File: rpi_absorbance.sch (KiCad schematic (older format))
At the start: 31 parts, among them P1 CONN_01X02, P2 CONN_01X06, P3 RPI_HEADER, Q1 NPN, U1 R-78B5.0-1.5L, U2 MEE1S1212SC, U3 DRV8825, U4 TCA9406DCUR

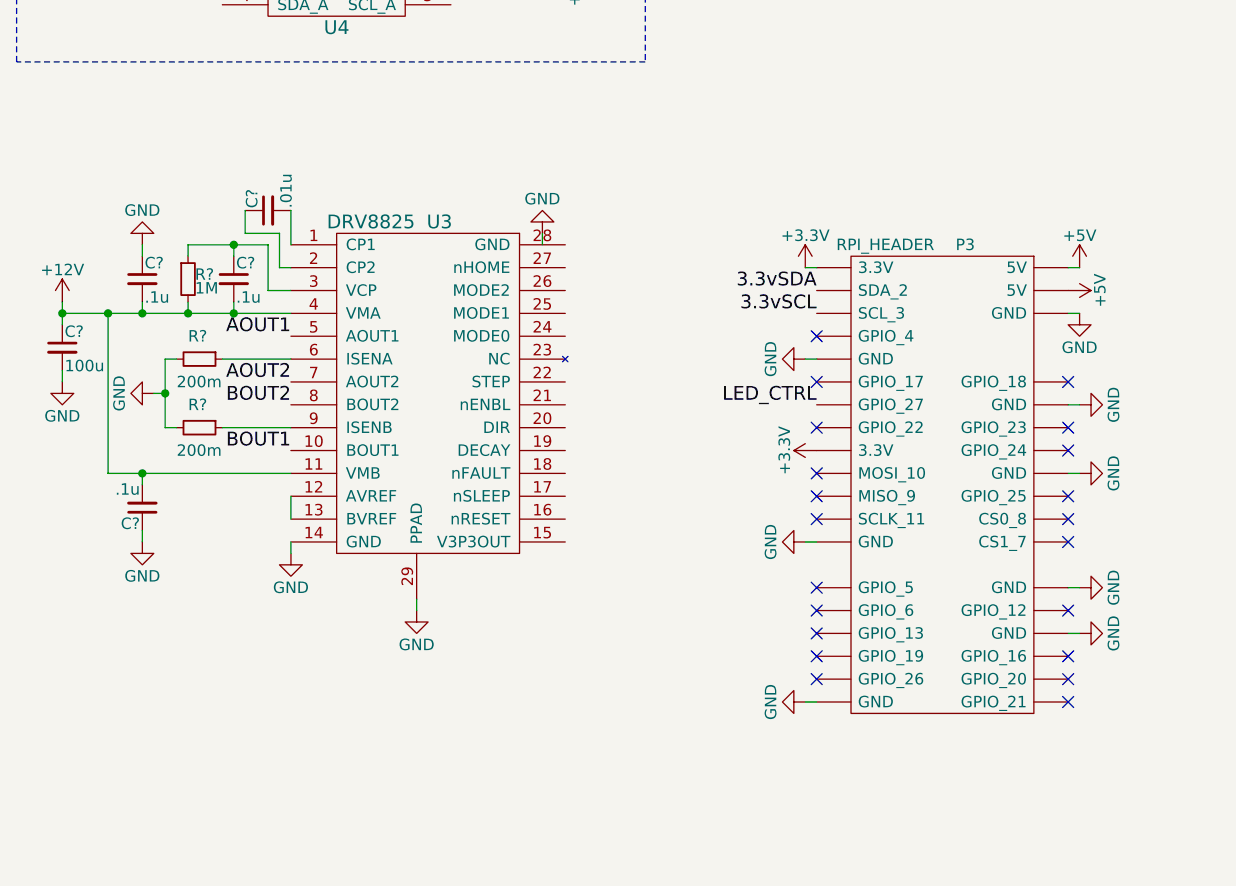
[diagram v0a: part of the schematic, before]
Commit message: Add stepper driver circuit
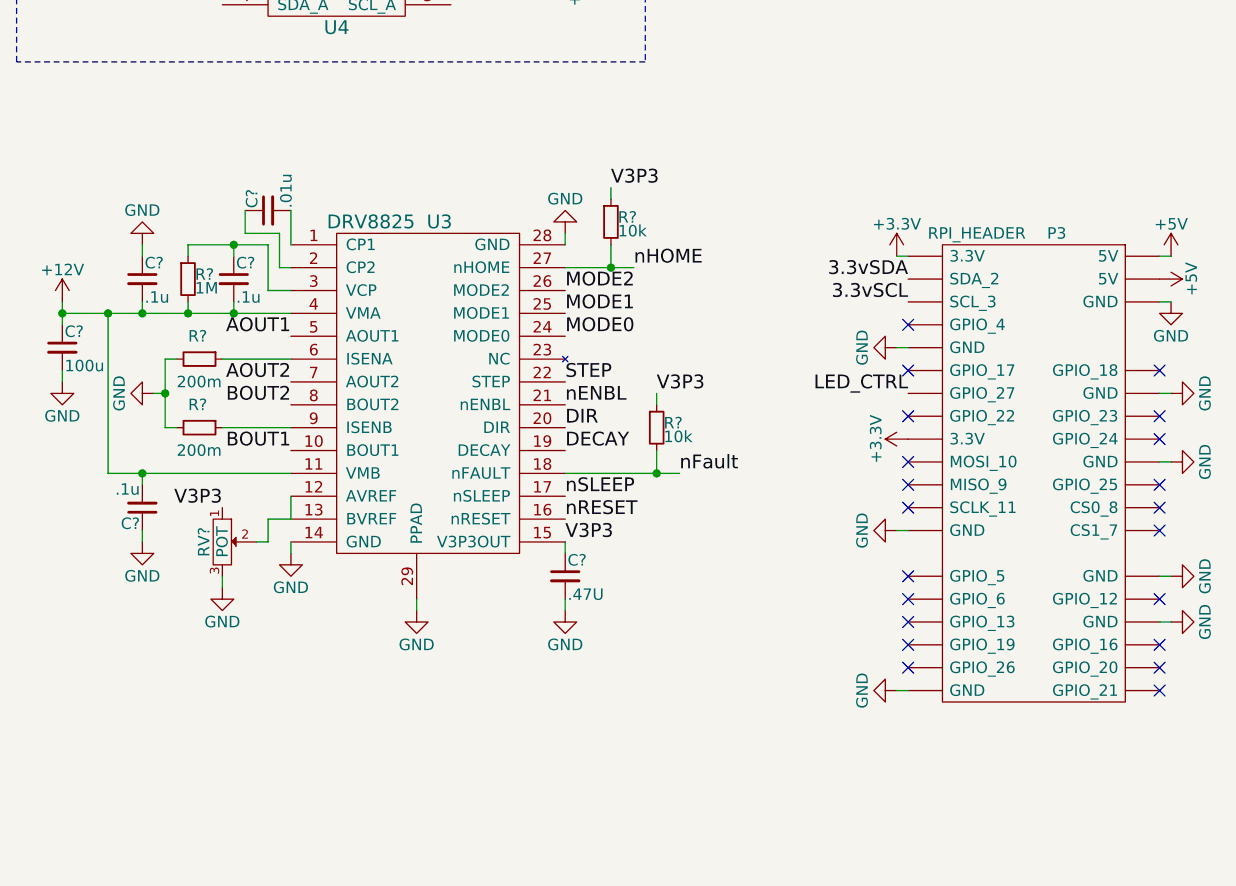
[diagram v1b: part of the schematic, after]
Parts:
- added C?: .47U, symbol C_Small
- added R? (x2): 10k, symbol R_Small
- added RV?: POT, symbol POT
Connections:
- net GND: now also U3.28 (GND), C?.2, RV?.3
- net at U3.12 (AVREF), U3.13 (BVREF): now also RV?.2
- net V3P3: now reaches U3.15 (V3P3OUT)
- net V3P3: now also C?.1, R?.1, R?.1, RV?.1
- net nRESET: now reaches U3.16 (nRESET)
- net nSLEEP: now reaches U3.17 (nSLEEP)
- net nFault: now reaches U3.18 (nFAULT)
- net nFault: now also R?.2
- net DECAY: now reaches U3.19 (DECAY)
- net DIR: now reaches U3.20 (DIR)
- net nENBL: now reaches U3.21 (nENBL)
- net STEP: now reaches U3.22 (STEP)
- net MODE0: now reaches U3.24 (MODE0)
- net MODE1: now reaches U3.25 (MODE1)
- net MODE2: now reaches U3.26 (MODE2)
- net nHOME: now reaches U3.27 (nHOME)
- net nHOME: now also R?.2
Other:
- moved on the sheet: P3

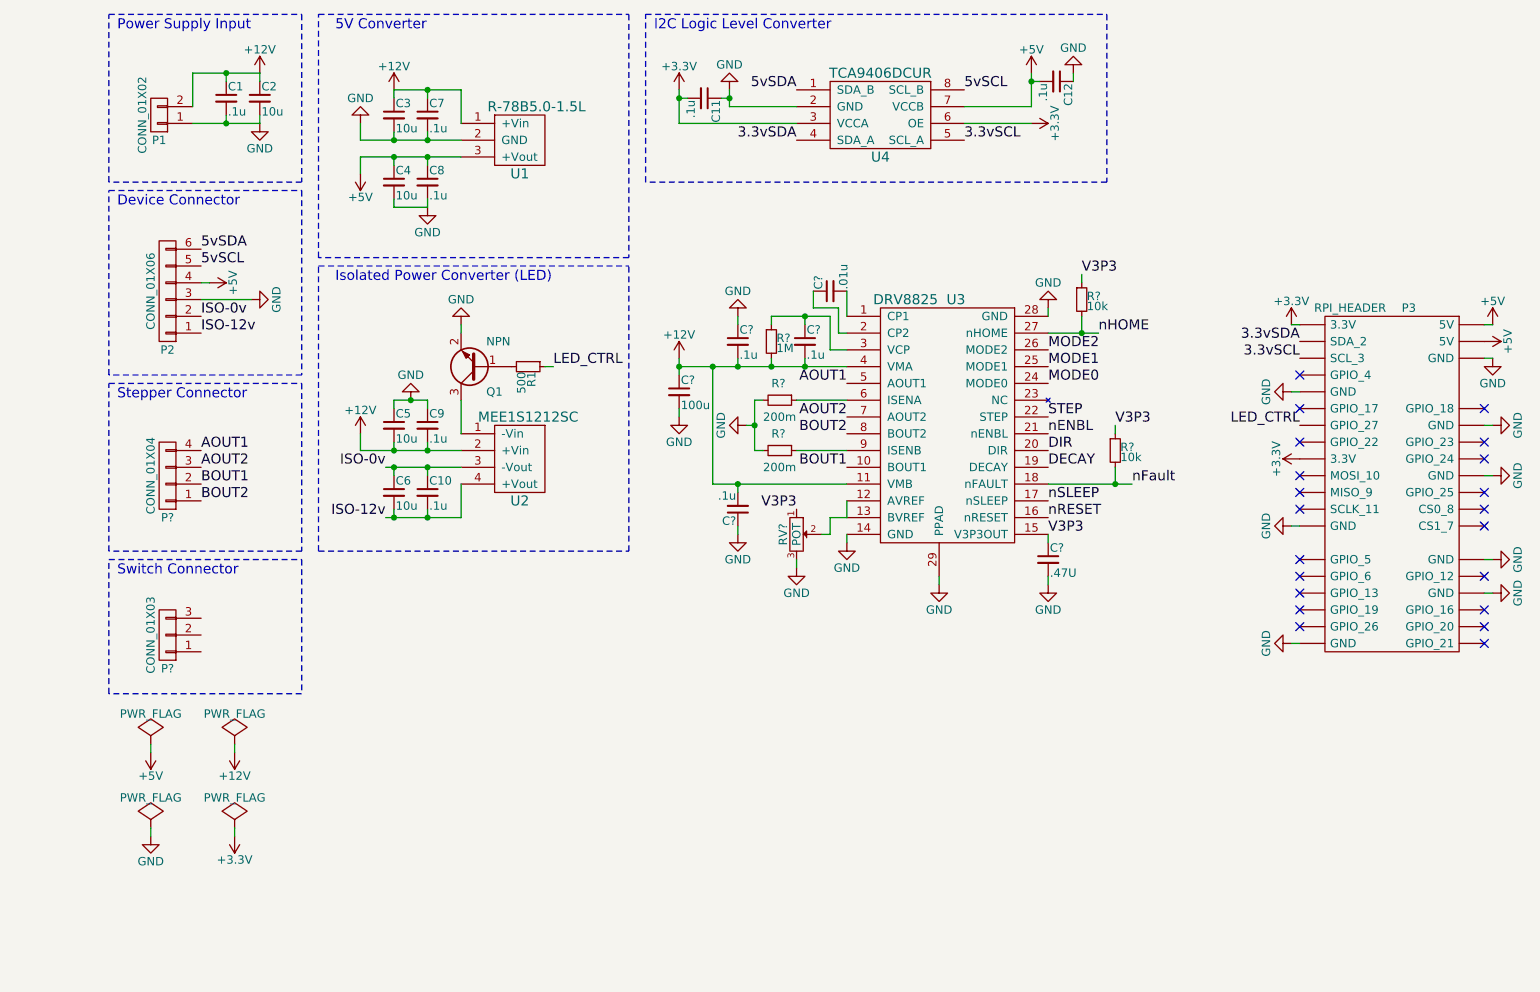
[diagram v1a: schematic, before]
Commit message: Connect raspberry pi header
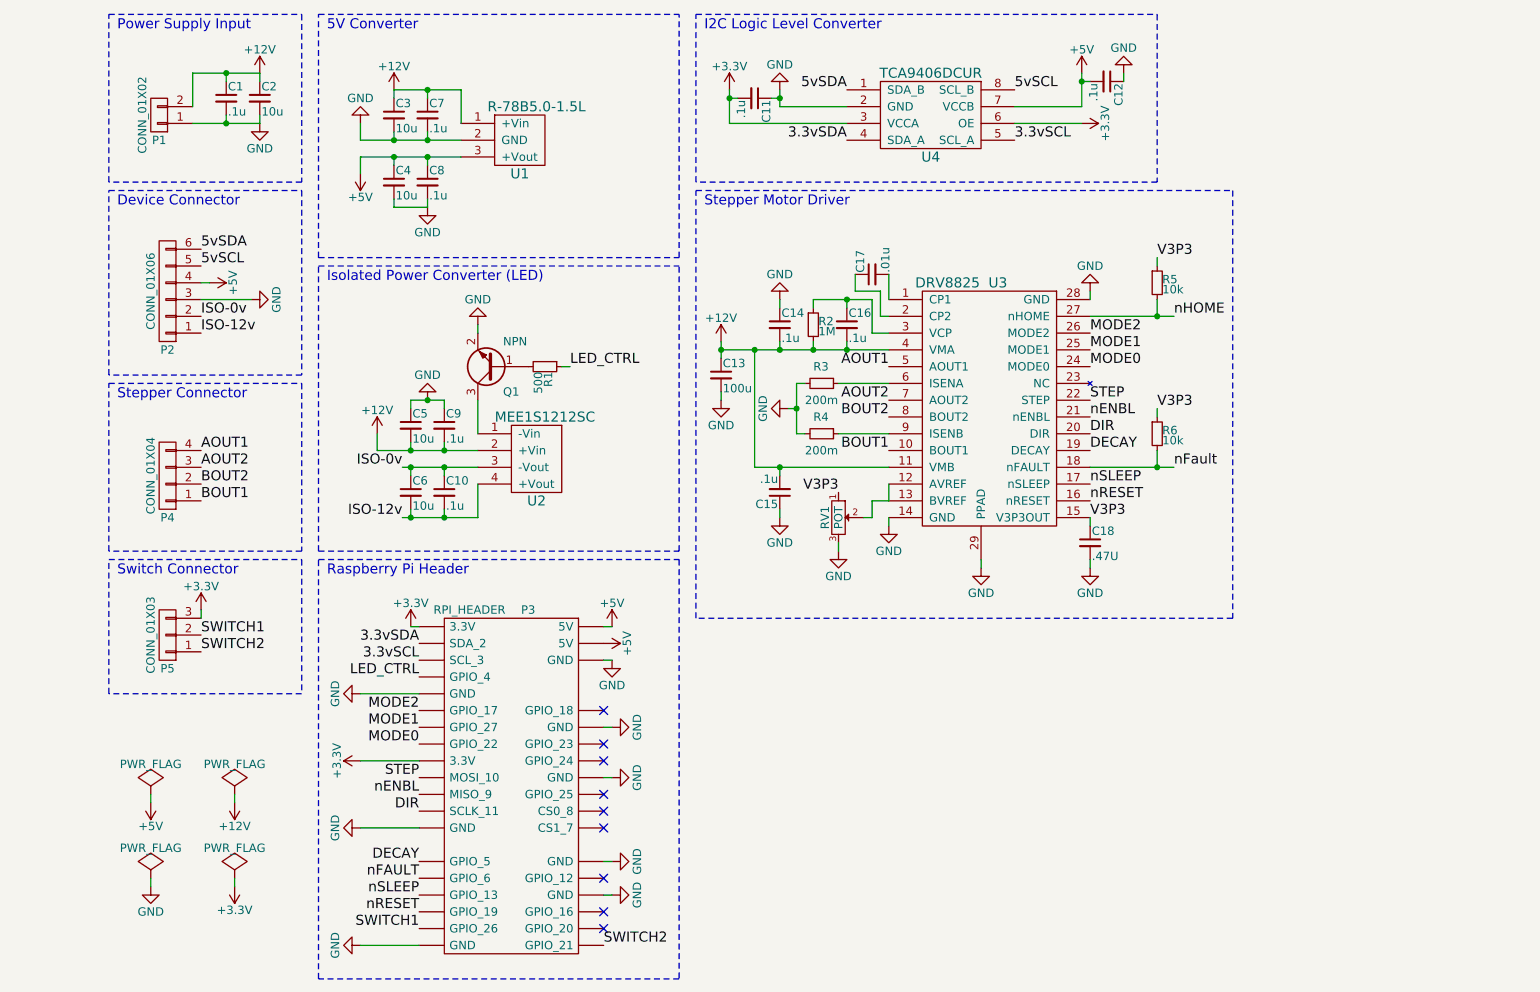
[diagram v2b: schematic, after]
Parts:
- gave numbers to parts that had none: 14
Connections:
- net +3V3: now also P5.3 (P3)
- net BOUT1: now also P4.1 (P1); no longer P4.2 (P2)
- net BOUT2: now also P4.2 (P2); no longer P4.1 (P1)
- net DECAY: now also P3.29 (GPIO_5)
- net DIR: now also P3.23 (SCLK_11)
- net LED_CTRL: now also P3.7 (GPIO_4); no longer P3.13 (GPIO_27)
- net MODE0: now also P3.15 (GPIO_22)
- net MODE1: now also P3.13 (GPIO_27)
- net MODE2: now also P3.11 (GPIO_17)
- net STEP: now also P3.19 (MOSI_10)
- net nENBL: now also P3.21 (MISO_9)
- net nRESET: now also P3.35 (GPIO_19)
- net nSLEEP: now also P3.33 (GPIO_13)
- net nFAULT: now reaches P3.31 (GPIO_6)
- net SWITCH1: now reaches P3.37 (GPIO_26)
- net SWITCH1: now also P5.2 (P2)
- net SWITCH2: now reaches P3.40 (GPIO_21)
- net SWITCH2: now also P5.1 (P1)
- no-connect marks 21 -> 9
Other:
- note added: "Raspberry Pi Header"
- note added: "Stepper Motor Driver"
- moved on the sheet: C10, C11, C12, C13, C14, C15, C16, C17, C18, C5, C6, C9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

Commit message: Add components
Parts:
- removed P1: CONN_01X02, symbol CONN_01X02
- removed P2: CONN_01X06, symbol CONN_01X06
- added CON1: BARREL_JACK, footprints:CUI_BARREL_JACK, symbol BARREL_JACK
- added P1: CONN_01X06, Pin_Headers:Pin_Header_Straight_1x06, symbol CONN_01X06
- added R7, R8: 10k, Resistors_SMD:R_0805_HandSoldering, symbol R_Small
- C1, C10, C11, C12, C14, C15, C16, C17, C18, C2, C3, C4, C5, C6, C7, C8, C9: footprint (none) -> Capacitors_SMD:C_0603
- C13: footprint (none) -> Capacitors_SMD:c_elec_8x6.7
- P3: footprint (none) -> Pin_Headers:Pin_Header_Straight_2x20
- P4: value CONN_01X04 -> stepper_conn; footprint (none) -> Pin_Headers:Pin_Header_Straight_1x04
- P5: value CONN_01X03 -> switch_conn; footprint (none) -> Pin_Headers:Pin_Header_Straight_1x03
- Q1: footprint (none) -> TO_SOT_Packages_SMD:SOT-23
- R1, R2, R3, R4, R5, R6: footprint (none) -> Resistors_SMD:R_0603
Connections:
- net +12V: now also CON1.1
- net +3V3: now also R7.1
- net +5V: now also P1.2 (P2), R8.1
- net 5vSCL: now also P1.4 (P4), R8.2
- net 5vSDA: now also P1.3 (P3), R7.2
- net GND: now also CON1.2, P1.1 (P1)
- net ISO-0v: now also P1.5 (P5)
- net ISO-12v: now also P1.6 (P6)
- no-connect marks 9 -> 10
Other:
- moved on the sheet: C11, C12, P5, U4
